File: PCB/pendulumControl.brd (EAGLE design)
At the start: 61.9 x 41.9 mm, 27 parts, among them IC1 PIC32MX340F512H, IC2 LT1963EST-3.3

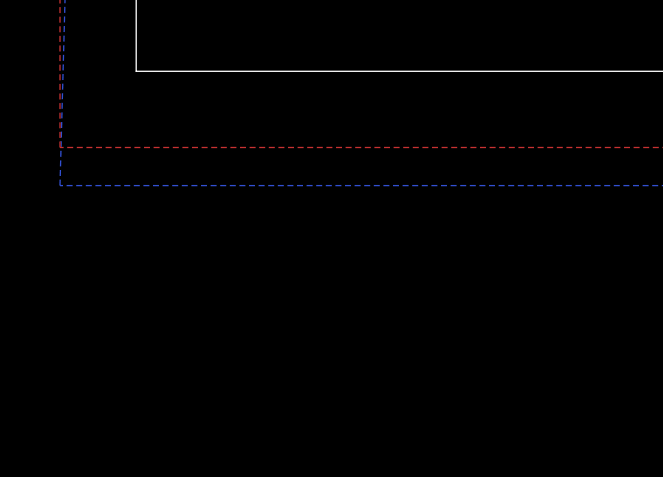
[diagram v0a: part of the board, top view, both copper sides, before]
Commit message: Added oscillator
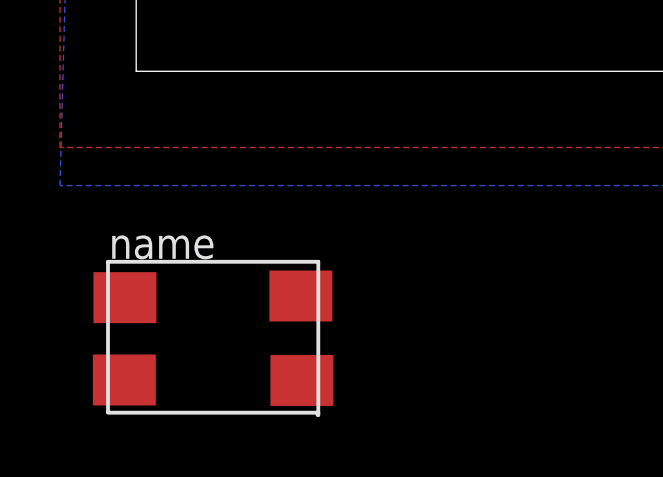
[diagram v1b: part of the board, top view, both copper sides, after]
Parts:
- added U$1: 7X5MMOSC, custom:7X5MMOSC
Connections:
- net GND: now also U$1.GND1, U$1.GND2
- net N$3: now also U$1.C1
- net OSC1: now also U$1.C2
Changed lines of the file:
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@@
 <element name="R6" library="rcl" package="R0805" value="" x="74.93" y="29.21" rot="MR0"/>
 <element name="R7" library="rcl" package="R0805" value="" x="74.93" y="24.13" rot="MR0"/>
+<element name="U$1" library="custom" package="7X5MMOSC" value="7X5MMOSC" x="25.4" y="-8.89"/>
 </elements>
 <signals>
@@
 <vertex x="20.32" y="-3.81"/>
 </polygon>
+<contactref element="U$1" pad="GND1"/>
+<contactref element="U$1" pad="GND2"/>
 <wire x1="66.04" y1="33.5788" x2="66.36" y2="36.83" width="0" layer="19" extent="1-1"/>
 <wire x1="66.04" y1="27.381" x2="66.04" y2="33.5788" width="0" layer="19" extent="1-1"/>
@@
 <wire x1="39.37" y1="20" x2="45.1" y2="20.07" width="0" layer="19" extent="1-1"/>
 <wire x1="43.18" y1="9.84" x2="48.55" y2="14.62" width="0" layer="19" extent="1-16"/>
+<wire x1="39.37" y1="11.11" x2="43.18" y2="9.84" width="0" layer="19" extent="16-16"/>
+<wire x1="54.61" y1="3.81" x2="51.75" y2="11.43" width="0" layer="19" extent="1-1"/>
 <wire x1="76.42" y1="21.59" x2="68.58" y2="16.83" width="0" layer="19" extent="1-1"/>
 <wire x1="76.42" y1="26.67" x2="76.42" y2="21.59" width="0" layer="19" extent="1-1"/>
+<wire x1="80.01" y1="11.43" x2="76.42" y2="21.59" width="0" layer="19" extent="1-1"/>
+<wire x1="81.28" y1="3.81" x2="80.01" y2="11.43" width="0" layer="19" extent="1-1"/>
+<wire x1="68.58" y1="3.81" x2="81.28" y2="3.81" width="0" layer="19" extent="1-1"/>
+<wire x1="50.8" y1="32.07" x2="56.5" y2="20.57" width="0" layer="19" extent="1-16"/>
+<wire x1="26.67" y1="26.67" x2="39.37" y2="20" width="0" layer="19" extent="1-1"/>
+<wire x1="36.83" y1="38.354" x2="50.8" y2="32.07" width="0" layer="19" extent="16-16"/>
+<wire x1="28.35" y1="-7.49" x2="39.37" y2="11.11" width="0" layer="19" extent="1-16"/>
+<wire x1="22.465" y1="-10.29" x2="28.35" y2="-7.49" width="0" layer="19" extent="1-1"/>
 </signal>
 <signal name="MCLR">
@@
 <contactref element="R3" pad="2"/>
 <contactref element="C5" pad="1"/>
+<contactref element="U$1" pad="C1"/>
 <wire x1="70.17" y1="12.7" x2="68.58" y2="18.73" width="0" layer="19" extent="1-1"/>
+<wire x1="22.485" y1="-7.545" x2="70.17" y2="12.7" width="0" layer="19" extent="1-1"/>
 </signal>
 <signal name="OSC2">
@@
 </signal>
 <signal name="OSC1">
+<contactref element="IC1" pad="39"/>
+<contactref element="U$1" pad="C2"/>
 <contactref element="C6" pad="1"/>
-<contactref element="IC1" pad="39"/>
-<wire x1="56.5" y1="19.57" x2="62.23" y2="13.02" width="0" layer="19" extent="1-1"/>
+<wire x1="62.23" y1="13.02" x2="56.5" y2="19.57" width="0" layer="19" extent="1-1"/>
+<wire x1="28.385" y1="-10.305" x2="56.5" y2="19.57" width="0" layer="19" extent="1-1"/>
 </signal>
 <signal name="RX">

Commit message: Completed first routing.
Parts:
- moved JP3 72.6 mm to (22.9, 47.0)
- moved JP4 71.6 mm to (11.4, 47.0)
- moved C5 66.5 mm to (5.55, 39.0), flipped to the bottom
- moved R3 63.7 mm to (11.2, 34.2), flipped to the bottom, turned to 270 degrees
- moved JP2 60.3 mm to (2.54, 34.3), turned to 90 degrees
- moved JP7 59.2 mm to (31.8, 45.7), flipped to the bottom, turned to 0 degrees
- moved C6 52.0 mm to (16.7, 39.1), flipped to the bottom
- moved R6 51.2 mm to (24.9, 18.1)
- moved U$1 50.0 mm to (11.2, 39.0)
- moved LED1 49.4 mm to (29.3, 15.7), turned to 270 degrees
- moved LED2 48.3 mm to (29.3, 18.0), turned to 270 degrees
- moved R7 46.0 mm to (29.1, 20.2), turned to 180 degrees
- moved IC2 43.6 mm to (22.9, 36.8)
- moved C9 39.5 mm to (27.9, 39.4), flipped to the bottom, turned to 0 degrees
- moved R2 35.9 mm to (6.35, 27.9), flipped to the bottom
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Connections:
- removed net AVDD: IC1.19
- net VCC3V3: now also IC1.19
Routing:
- net GND: track 0.00 -> 49.9 mm, vias 0 -> 4
- net M_CHA: track 0.00 -> 45.4 mm, vias 0 -> 3
- net LIM_R: track 0.00 -> 45.0 mm, vias 0 -> 3
- net LIM_L: track 0.00 -> 42.6 mm, vias 0 -> 1
- net ARM_CHA: track 0.00 -> 40.4 mm, vias 0 -> 3
- net ARM_CHB: track 0.00 -> 35.5 mm, vias 0 -> 4
- net M_CHB: track 0.00 -> 31.9 mm, vias 0 -> 2
- net RX: track 0.00 -> 28.8 mm, vias 0 -> 2
- net TX: track 0.00 -> 27.0 mm, vias 0 -> 1
- net OSC1: track 0.00 -> 23.2 mm, vias 0 -> 5
- net OSC2: track 0.00 -> 17.0 mm, vias 0 -> 1
- net N$3: track 0.00 -> 15.4 mm, vias 0 -> 1
- net MCLR: track 0.00 -> 14.5 mm, vias 0 -> 1
- net VCC3V3: track 0.00 -> 13.5 mm, vias 0 -> 2
- net P32_PGC: track 0.00 -> 9.87 mm, vias 0 -> 1
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- added copper zone on layer 1, net VCC5V
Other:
- board size 61.9 x 41.9 mm -> 37.8 x 37.4 mm

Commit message: Fixed Header on wrong side of board
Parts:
- JP2: device SparkFun-Connectors:1X04_LOCK_LONGPADS -> SparkFun-Connectors:1X04
- moved JP7 3.48 mm to (28.3, 45.7), flipped to the top
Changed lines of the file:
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@@
 </element>
 <element name="JP1" library="SparkFun-Connectors" package="1X06_FEMALE_LOCK.010" value="" x="2.54" y="17.78" rot="R90"/>
-<element name="JP2" library="SparkFun-Connectors" package="1X04_LOCK_LONGPADS" value="" x="2.54" y="34.29" rot="R90"/>
+<element name="JP2" library="SparkFun-Connectors" package="1X04" value="" x="2.54" y="34.29" rot="R90"/>
 <element name="JP3" library="SparkFun-Connectors" package="1X04" value="" x="22.86" y="46.99" rot="R180"/>
 <element name="JP4" library="SparkFun-Connectors" package="1X04" value="" x="11.43" y="46.99" rot="R180"/>
 <element name="JP5" library="SparkFun-Connectors" package="1X03" value="" x="33.02" y="21.59" rot="R90"/>
 <element name="JP6" library="SparkFun-Connectors" package="1X04" value="" x="33.02" y="31.75" rot="R90"/>
-<element name="JP7" library="SparkFun-Connectors" package="SCREWTERMINAL-3.5MM-2" value="" x="31.75" y="45.72" rot="MR0">
-<attribute name="PROD_ID" value="CONN-08399" x="31.75" y="45.72" size="1.778" layer="28" rot="MR0" display="off"/>
+<element name="JP7" library="SparkFun-Connectors" package="SCREWTERMINAL-3.5MM-2" value="" x="28.273675" y="45.72">
+<attribute name="PROD_ID" value="CONN-08399" x="28.273675" y="45.72" size="1.778" layer="27" display="off"/>
 </element>
 <element name="LED1" library="led" package="CHIP-LED0805" value="" x="29.32273125" y="15.689728125" rot="R270"/>
@@
 <wire x1="13.47931875" y1="27.7609375" x2="10.922" y2="28.956" width="0.254" layer="16"/>
 <wire x1="10.922" y1="28.956" x2="10.668" y2="28.956" width="0.254" layer="16"/>
-<wire x1="10.668" y1="28.956" x2="2.794" y2="36.83" width="0.254" layer="16"/>
+<wire x1="10.668" y1="28.956" x2="2.54" y2="36.83" width="0.254" layer="16"/>
 </signal>
 <signal name="M_CHB">

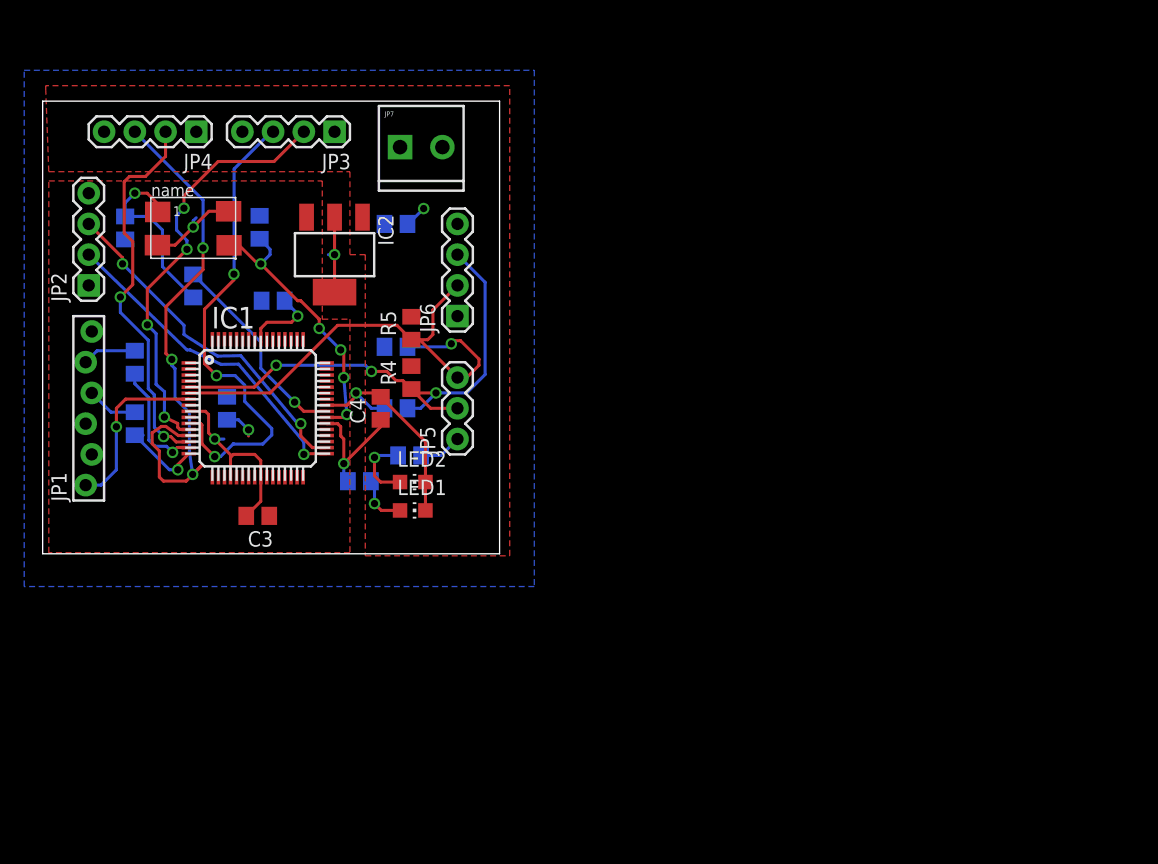
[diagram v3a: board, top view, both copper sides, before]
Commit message: Changed Crystal and power input. Crystal now has clear zone.
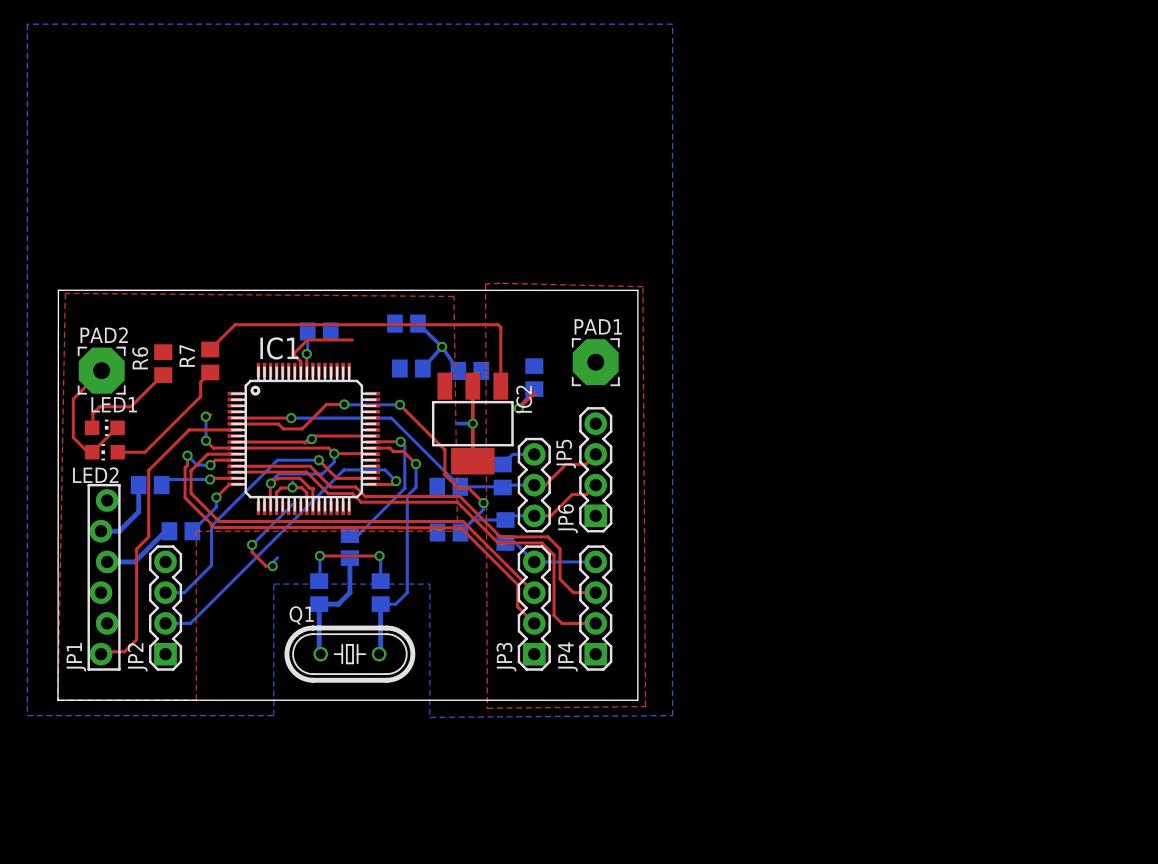
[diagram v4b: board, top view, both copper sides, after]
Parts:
- removed JP7: (no value), SparkFun-Connectors:SCREWTERMINAL-3.5MM-2
- removed U$1: 7X5MMOSC, custom:7X5MMOSC
- added PAD1, PAD2: (no value), wirepad:3,81/1,4
- added Q1: (no value), crystal:HC49/S
- moved JP4 54.4 mm to (44.5, 3.81), turned to 90 degrees
- moved JP3 46.2 mm to (39.4, 3.81), turned to 90 degrees
- moved C5 34.1 mm to (21.6, 8.89), turned to 90 degrees
- moved C6 31.8 mm to (26.7, 8.89)
- moved JP2 31.1 mm to (8.89, 3.81)
- moved LED1 26.3 mm to (3.87, 22.5)
- moved LED2 25.6 mm to (3.89, 20.5), turned to 90 degrees
- moved R3 25.1 mm to (24.1, 12.7)
- moved C2 20.3 mm to (34.0, 27.2), turned to 180 degrees
- moved JP6 20.1 mm to (44.5, 15.2)
- moved R6 18.9 mm to (8.70, 27.8), flipped to the top, turned to 90 degrees
- moved R5 18.5 mm to (37.0, 14.0), flipped to the bottom, turned to 270 degrees
- moved R7 18.2 mm to (12.6, 28.0), flipped to the top, turned to 90 degrees
- moved IC2 18.1 mm to (34.3, 22.9)
- moved C3 17.6 mm to (29.2, 27.4), flipped to the bottom, turned to 0 degrees
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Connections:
- net GND: now also PAD2.1; no longer JP7.1, U$1.GND1, U$1.GND2
- net N$3: now also Q1.1; no longer U$1.C1
- net OSC1: now also Q1.2; no longer U$1.C2
- net VCC5V: now also PAD1.1; no longer JP7.2
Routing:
- net VCC5V: track 5.79 -> 44.7 mm
- net VCC3V3: track 13.5 -> 45.8 mm, vias 2 -> 5
- net MCLR: track 14.5 -> 26.4 mm, vias 1 -> 0
- net LIM_R: track 45.0 -> 33.3 mm, vias 3 -> 1
- net M_CHA: track 45.4 -> 35.7 mm, vias 3 -> 0
- net ARM_CHB: track 35.5 -> 42.2 mm, vias 4 -> 2
- net M_CHB: track 31.9 -> 37.9 mm, vias 2 -> 0
- net N$3: track 15.4 -> 10.1 mm, vias 1 -> 0
- net N$5: track 5.86 -> 11.1 mm, vias 1 -> 0
- net RX: track 28.8 -> 24.2 mm, vias 2 -> 1
- net OSC2: track 17.0 -> 12.5 mm
- net GND: track 49.9 -> 54.4 mm, vias 4 -> 7
- net N$4: track 4.32 -> 8.34 mm, vias 1 -> 0
- net P32_PGC: track 9.87 -> 6.28 mm
- net N$10: track 6.09 -> 3.22 mm
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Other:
- board size 37.8 x 37.4 mm -> 47.9 x 33.9 mm
